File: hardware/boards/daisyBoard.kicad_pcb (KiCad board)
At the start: 4 copper layers, 100 x 100 mm, 93 parts, among them IC1 TL072, IC2 TL072, IC3 TL072, IC4 TL072, J1 LEFT Pin ROW, J12 Micro_SD_Card, J13 LEFT Pin ROW Daisy, J14 RIGHT Pin ROW DAISY, J15 Daisy Pin Breakout LEFT, J16 Daisy PIN Breakout RIGHT, J2 RIGHT Pin Row, J3 ESP32 Pin Breakout RIGHT, J4 ESP32 Pin Breakout LEFT, J5 Micro_SD_Card, U1 MCP6002-xSN, U2 MCP6002-xSN, U3 MCP6002-xSN

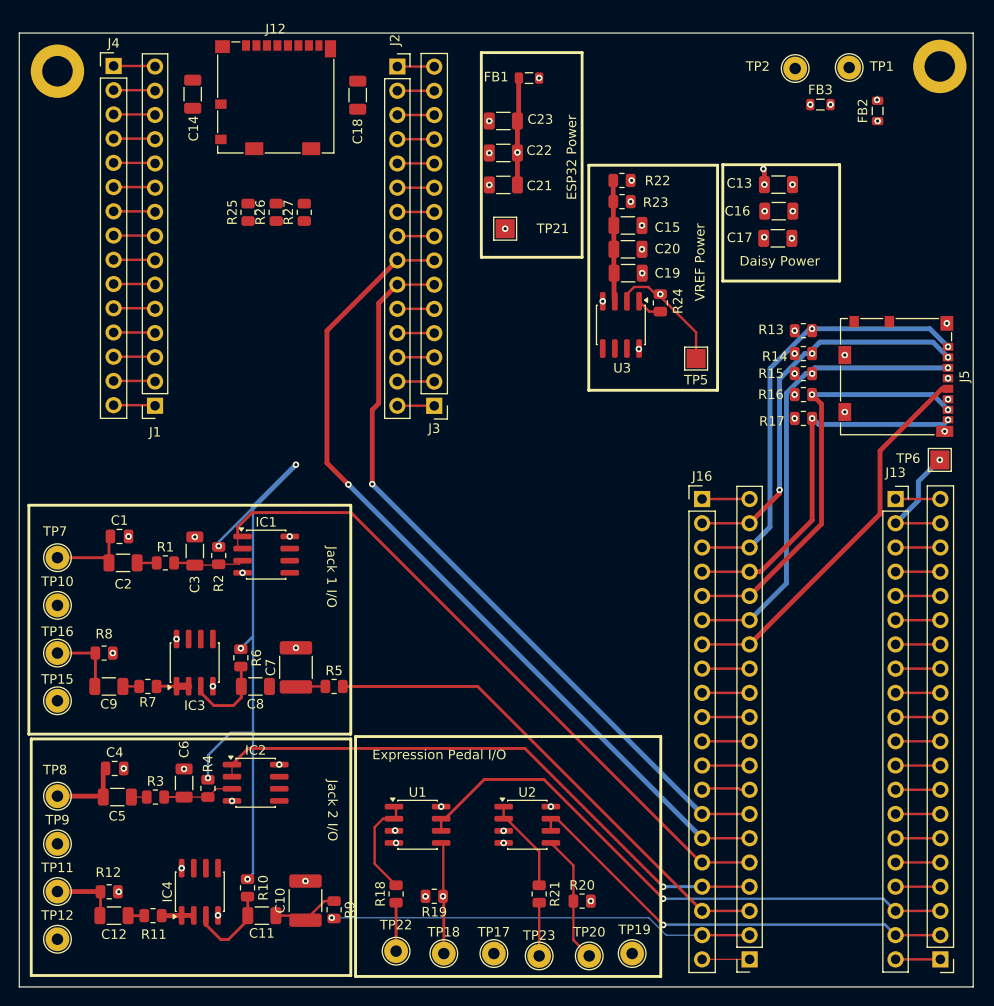
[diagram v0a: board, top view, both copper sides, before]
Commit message: Added compatible components
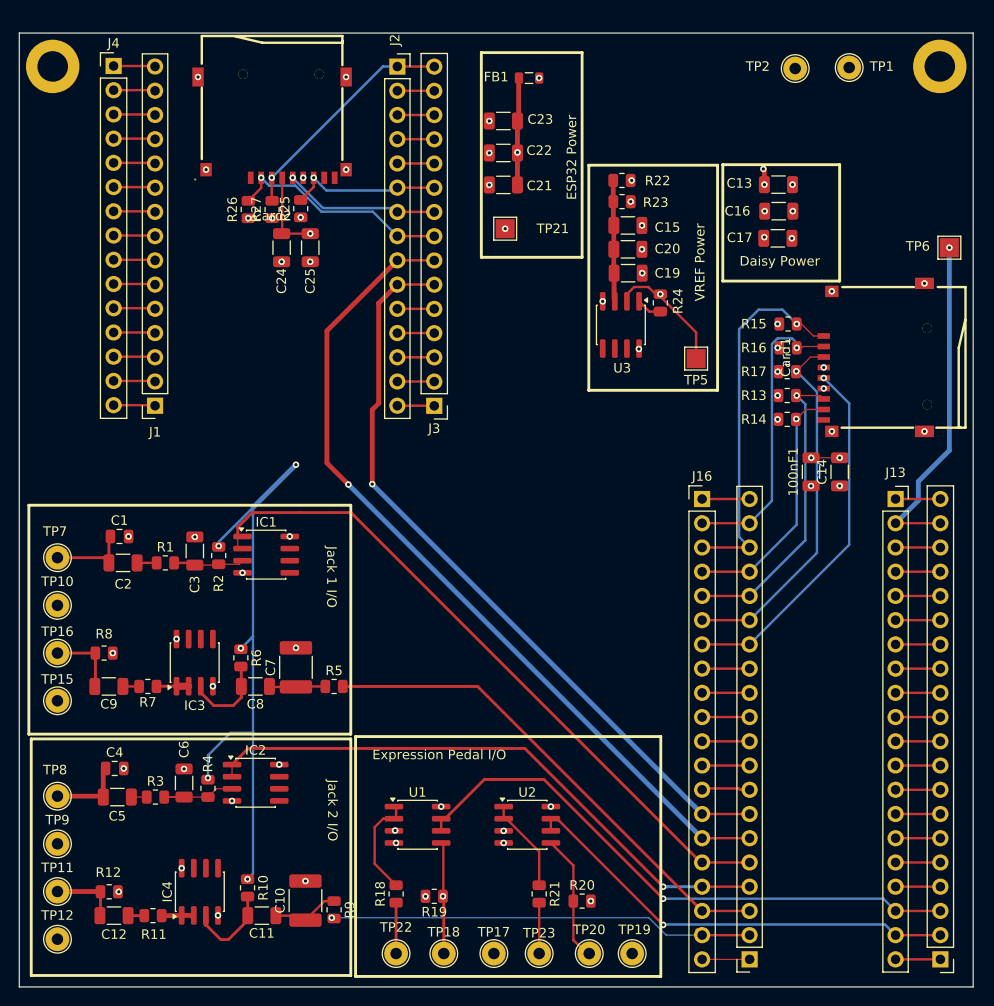
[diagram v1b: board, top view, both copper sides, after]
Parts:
- removed C18: 10uF, Capacitor_SMD:C_1206_3216Metric
- removed FB2, FB3: 600R @ 100MHz, Inductor_SMD:L_0805_2012Metric
- removed J12, J5: Micro_SD_Card, Connector_Card:microSD_HC_Molex_104031-0811
- added 100nF1: C26, Capacitor_SMD:C_1206_3216Metric, F.Cu at (133.0, 96.0)
- added C24: 10uF, Capacitor_SMD:C_1206_3216Metric, F.Cu at (77.5, 72.5)
- added C25: 100nF, Capacitor_SMD:C_1206_3216Metric, F.Cu at (80.5, 72.5)
- added Card1: TF-01A, lcsc_footprints:C91145_TF-SMD_TF-01A, F.Cu at (139.6, 84.0)
- added Card2: TF-01A, lcsc_footprints:C91145_TF-SMD_TF-01A, F.Cu at (76.5, 59.9)
- C14: value 0.1uF -> 10uF
- FB1: value 600R @ 100MHz -> 60R @ 100MHz
- R13, R14, R15, R16, R17, R25, R26, R27: value 10K -> 47K
- moved C14 78.5 mm to (136.0, 96.0)
- moved TP6 22.3 mm to (147.5, 72.5)
- moved R14 7.11 mm to (130.5, 90.5)
- moved R13 7.01 mm to (130.5, 88.0)
- moved R25 5.54 mm to (79.5, 68.4)
- moved R15 5.44 mm to (130.6, 80.5)
- moved R17 5.19 mm to (130.5, 85.5)
- moved R16 5.16 mm to (130.6, 83.0)
- moved R27 3.39 mm to (76.5, 68.5)
- moved R26 2.94 mm to (74.0, 68.5)
- moved REF** 0.71 mm to (53.5, 53.5)
- moved TP20 0.25 mm to (109.8, 146.5)
- moved TP22 0.25 mm to (89.5, 146.5)
- moved TP23 0.25 mm to (104.5, 146.5)
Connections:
- C1 pad 2: GNDA -> GND
- C10 pad 2: GNDA -> GND
- C13 pad 2: GNDA -> GND
- C14 pad 1: GNDD -> GND
- C14 pad 2: ESP-3.3V -> +3.3VD
- C15 pad 2: GNDA -> GND
- C16 pad 2: GNDA -> GND
- C17 pad 2: GNDA -> GND
- C19 pad 2: GNDA -> GND
- C20 pad 2: GNDA -> GND
- C21 pad 2: GNDD -> GND
- C22 pad 2: GNDD -> GND
- C23 pad 2: GNDD -> GND
- C3 pad 1: GNDA -> GND
- C4 pad 2: GNDA -> GND
- C6 pad 1: GNDA -> GND
- C7 pad 2: GNDA -> GND
- IC1 pad 4: GNDA -> GND
- IC2 pad 4: GNDA -> GND
- IC3 pad 4: GNDA -> GND
- IC4 pad 4: GNDA -> GND
- J1 pad 2: GNDD -> GND
- J13 pad 1: GNDA -> GND
- J14 pad 1: GNDA -> GND
- J15 pad 20: GNDA -> GND
- J16 pad 20: GNDA -> GND
- J2 pad 14: GNDD -> GND
- J3 pad 2: GNDD -> GND
- J4 pad 14: GNDD -> GND
- R12 pad 2: GNDA -> GND
- R13 pad 2: /SD_DAT_2_DAISY -> /SD_DAT_0_DAISY
- R14 pad 2: /SD_DAT_3_DAISY -> /SD_DAT_1_DAISY
- R15 pad 2: /SD_CMD_DAISY -> /SD_DAT_2_DAISY
- R16 pad 2: /SD_DAT_0_DAISY -> /SD_DAT_3_DAISY
- R17 pad 2: /SD_DAT_1_DAISY -> /SD_CMD_DAISY
- R19 pad 2: GNDA -> GND
- R20 pad 2: GNDA -> GND
- R23 pad 1: GNDA -> GND
- R25 pad 2: /SD_CS -> /SD_MISO
- R26 pad 2: /SD_MOSI -> /SD_CS
- R27 pad 2: /SD_MISO -> /SD_MOSI
- R8 pad 2: GNDA -> GND
- TP10 pad 1: GNDA -> GND
- TP12 pad 1: GNDA -> GND
- TP15 pad 1: GNDA -> GND
- TP17 pad 1: GNDA -> GND
- TP19 pad 1: GNDA -> GND
- TP9 pad 1: GNDA -> GND
- U1 pad 4: GNDA -> GND
- U2 pad 4: GNDA -> GND
- U3 pad 4: GNDA -> GND
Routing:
- net +3.3VD: track 41.5 -> 65.8 mm, vias 6 -> 8
- net VCC_Daisy: track 90.8 -> 111.3 mm
- net /SD_MOSI: track 3.87 -> 24.3 mm, vias 0 -> 1
- net /SD_CS: track 4.59 -> 24.4 mm, vias 0 -> 1
- net /SD_DAT_1_DAISY: track 40.2 -> 27.1 mm, vias 2 -> 1
- net /SD_DAT_0_DAISY: track 44.7 -> 32.0 mm, vias 2 -> 1
- net /SD_SCK: track 3.87 -> 16.3 mm, vias 0 -> 1
- net /SD_MISO: track 3.87 -> 16.2 mm, vias 0 -> 1
- net /SD_DAT_3_DAISY: track 41.7 -> 31.3 mm, vias 3 -> 1
- net /SD_CMD_DAISY: track 48.7 -> 38.5 mm, vias 2 -> 1
- net GNDA: track 9.74 -> 0.00 mm, vias 30 -> 0
- net GND: track 9.78 -> 18.5 mm, vias 2 -> 41
- net ESP-3.3V: track 3.87 -> 12.2 mm, vias 0 -> 4
- net GNDD: track 8.29 -> 0.00 mm, vias 4 -> 0
- net /SD_DAT_2_DAISY: track 46.4 -> 39.3 mm, vias 2 -> 1
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- added copper zone on In2.Cu, net GND
- removed copper zone on In1.Cu, net +3.3VD
- removed copper zone on In2.Cu, net GNDA
- removed copper zone on In2.Cu, net GNDD

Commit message: updated design and added start for indicator leds on design
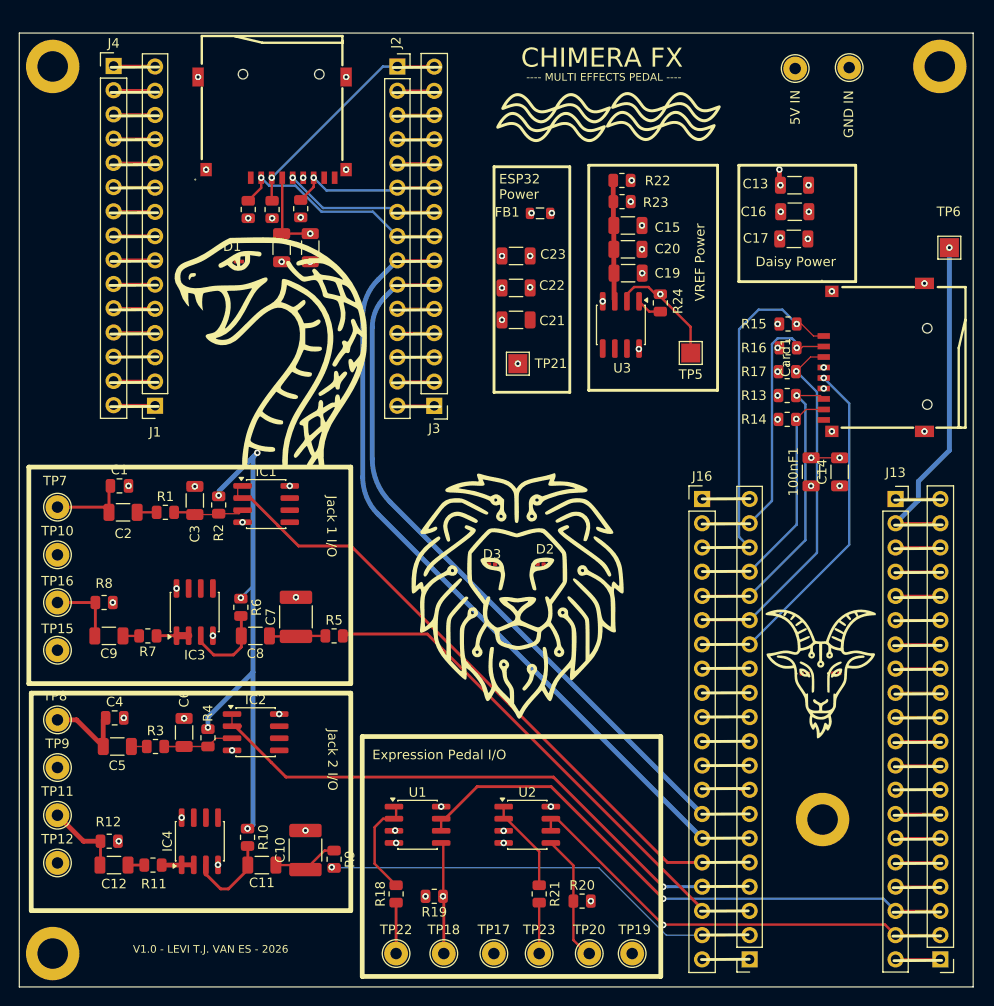
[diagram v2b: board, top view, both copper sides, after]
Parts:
- added D1: SNAKE EYE, LED_SMD:LED_0201_0603Metric, F.Cu at (73.0, 74.0)
- added D2: LION EYE 2, LED_SMD:LED_0201_0603Metric, F.Cu at (104.7, 105.7)
- added D3: LION EYE 1, LED_SMD:LED_0201_0603Metric, F.Cu at (99.6, 105.7)
- added D4: GOAT EYE 1, LED_SMD:LED_0201_0603Metric, F.Cu at (132.3, 117.2)
- added D5: GOAT EYE 2, LED_SMD:LED_0201_0603Metric, F.Cu at (135.6, 117.1)
- added G***: LOGO, LOGO, F.Cu at (105.8, 57.4)
- added G***: LOGO, LOGO, F.Cu at (133.8, 117.0)
- added G***: LOGO, LOGO, F.Cu at (116.7, 59.2)
- added G***: LOGO, LOGO, F.Cu at (117.3, 57.3)
- added G***: LOGO, LOGO, F.Cu at (105.2, 59.3)
- added G***: LOGO, LOGO, F.Cu at (76.6, 83.2)
- added G***: LOGO, LOGO, F.Cu at (101.8, 107.9)
- added REF**: MountingHole_3.2mm_M3_DIN965_Pad, MountingHole:MountingHole_3.2mm_M3_DIN965_Pad, F.Cu at (53.5, 146.5)
- added REF**: MountingHole_3.2mm_M3_DIN965_Pad, MountingHole:MountingHole_3.2mm_M3_DIN965_Pad, F.Cu at (134.2, 132.4)
- TP1: value Global Ground - Functional -> GND IN
- TP11: value Jack Output 2 Signal Pad -> Jack Output 2 Signal Pad test
- TP2: value Global power 5V Input field - Functional -> 5V IN
- moved FB1 14.2 mm to (104.6, 68.9)
- moved C23 14.2 mm to (102.1, 73.4)
- moved C21 14.2 mm to (102.1, 80.1)
- moved C22 14.2 mm to (102.1, 76.7)
- moved TP21 14.2 mm to (102.3, 84.7)
- moved TP11 8.00 mm to (54.0, 132.0)
- moved TP12 8.00 mm to (54.0, 137.0)
- moved TP8 8.00 mm to (54.0, 122.0)
- moved TP9 8.00 mm to (54.0, 127.0)
- moved C1 5.30 mm to (60.5, 97.5)
- moved C11 5.30 mm to (75.4, 137.2)
- moved C12 5.30 mm to (59.9, 137.2)
- moved C6 5.30 mm to (67.3, 123.3)
- moved IC1 5.30 mm to (75.9, 99.4)
- moved IC4 5.30 mm to (68.9, 134.7)
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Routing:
- net VCC_ESP32: track 86.4 -> 68.2 mm, vias 2 -> 4
- net +5V: track 81.8 -> 93.1 mm
- net /ESP_TO_DAISY: track 88.9 -> 85.2 mm, vias 1 -> 0
- net VREF: track 123.7 -> 120.9 mm
- net /AUDIO_OUT_1: track 52.5 -> 55.1 mm
- net /AUDIO_OUT_2: track 45.4 -> 47.6 mm
- net /AUDIO_IN_1: track 71.8 -> 70.3 mm
- net VCC_Daisy: track 111.3 -> 112.7 mm
- net /AUDIO_IN_2: track 62.3 -> 63.5 mm
- net Net-(C12-Pad2): track 7.05 -> 8.20 mm
- net Net-(C4-Pad1): track 7.94 -> 9.06 mm
- net /ADC_EXP_IN_1: track 61.4 -> 60.8 mm
- net /DAISY_TO_ESP: track 79.8 -> 79.3 mm, vias 1 -> 0
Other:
- board text added: "---- MULTI EFFECTS PEDAL ----"
- board text added: "CHIMERA FX"
- board text added: "V1.0 - LEVI T.J. VAN ES - 2026"

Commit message: removed grbrs and updated corner design pcb and still need to add led resistors
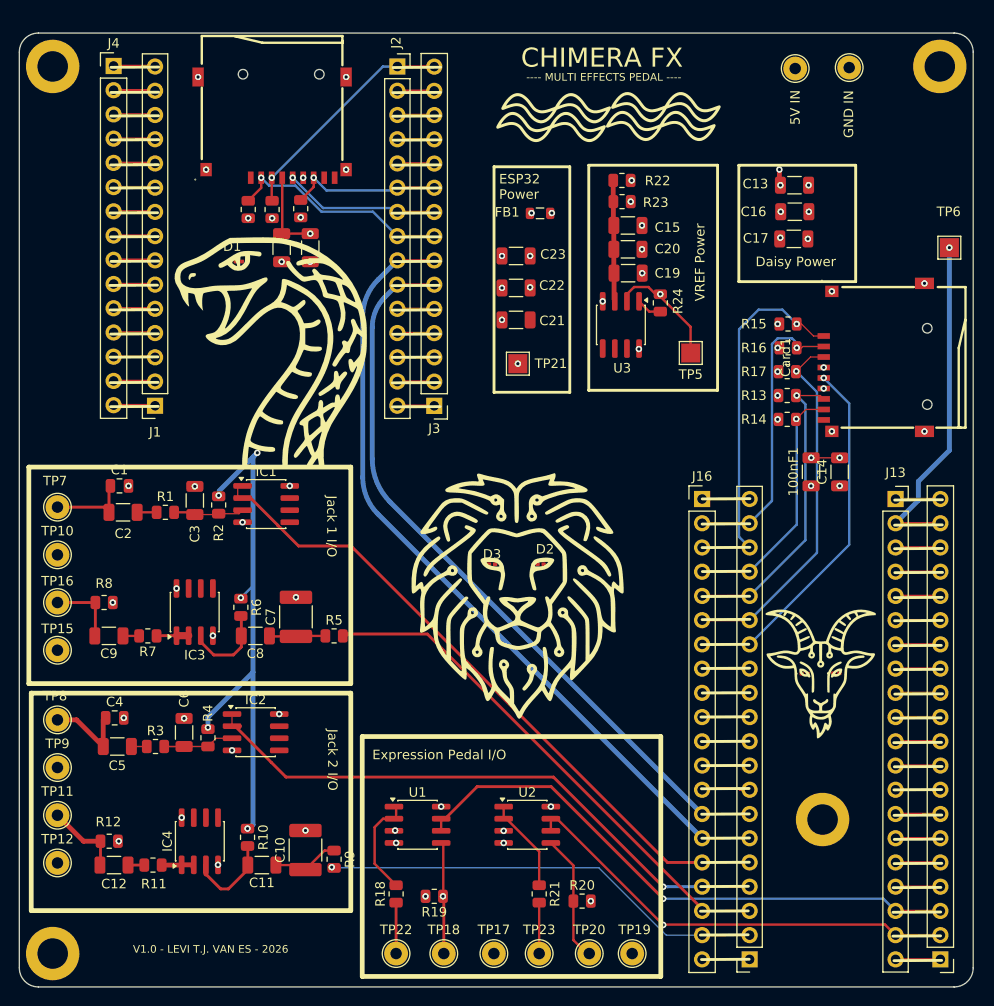
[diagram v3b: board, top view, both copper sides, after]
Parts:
- D1: value SNAKE EYE -> SNAKE EYE - GREEN
- D2: value LION EYE 2 -> LION EYE 2 - YELLOW
- D3: value LION EYE 1 -> LION EYE 1 - YELLOW
- D4: value GOAT EYE 1 -> GOAT EYE 1 - RED
- D5: value GOAT EYE 2 -> GOAT EYE 2 - RED
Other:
- outline, holes or cut-outs redrawn

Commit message: added led values
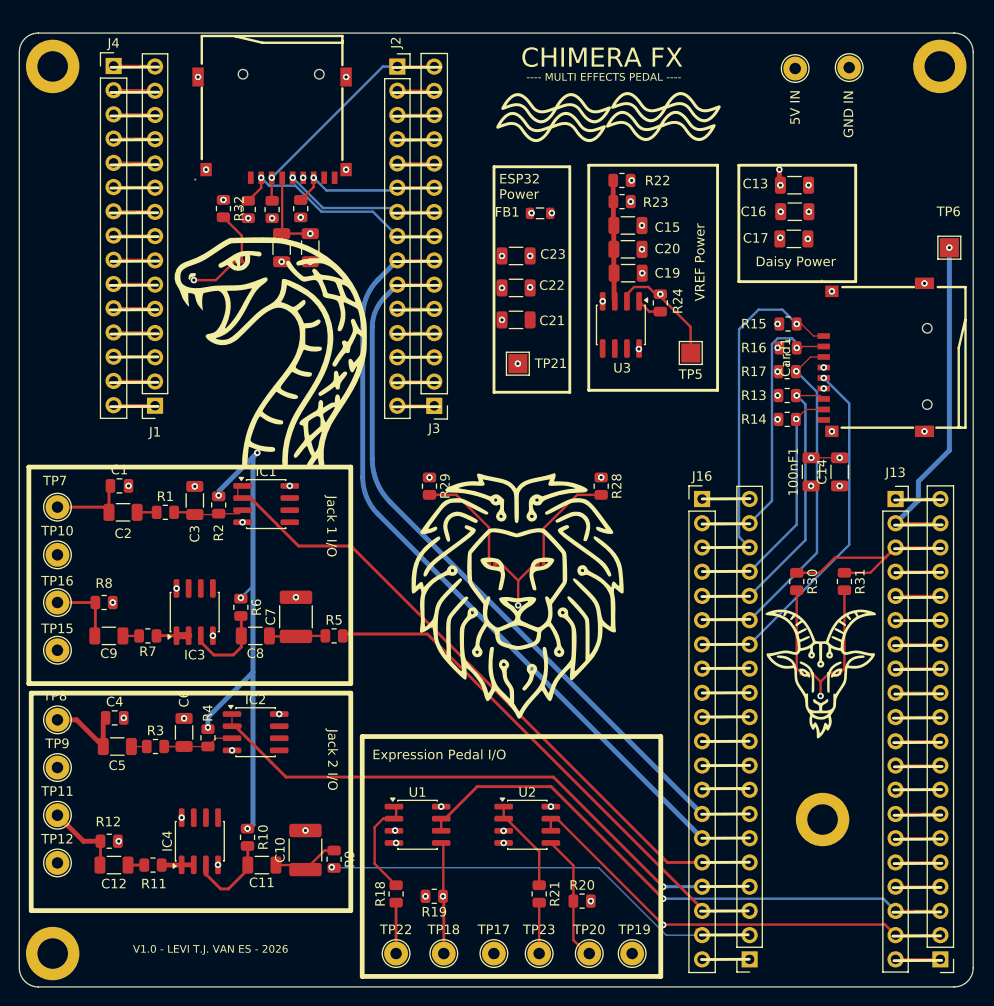
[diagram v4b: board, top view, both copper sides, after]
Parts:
- added R28: 150, Resistor_SMD:R_0805_2012Metric, F.Cu at (111.0, 97.5)
- added R29: 150, Resistor_SMD:R_0805_2012Metric, F.Cu at (93.0, 97.5)
- added R30: 120, Resistor_SMD:R_0805_2012Metric, F.Cu at (131.5, 107.5)
- added R31: 120, Resistor_SMD:R_0805_2012Metric, F.Cu at (136.5, 107.5)
- added R32: 27, Resistor_SMD:R_0805_2012Metric, F.Cu at (71.4, 68.4)
- D2: value LION EYE 2 - YELLOW -> LION EYE 2 - RED
- D3: value LION EYE 1 - YELLOW -> LION EYE 1 - RED
- D4: value GOAT EYE 1 - RED -> GOAT EYE 1 - YELLOW
- D5: value GOAT EYE 2 - RED -> GOAT EYE 2 - YELLOW
- R5, R9: value 3R3 -> 3K3
- TP21: value Processed input power at 5V ESP32 - Probe -> VCC_ESP32_Probe
- TP6: value Processed input power at 5V Daisy- Probe -> VCC Daisy Probe
- turned D3 to 180 degrees
- turned D4 to 180 degrees
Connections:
- D1 pad 2: ESP-3.3V -> Net-(D1-A)
- D2 pad 2: VCC_Daisy -> Net-(D2-A)
- D3 pad 2: VCC_Daisy -> Net-(D3-A)
- D4 pad 2: +3.3VD -> Net-(D4-A)
- D5 pad 2: +3.3VD -> Net-(D5-A)
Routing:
- net GND: track 18.5 -> 37.0 mm, vias 41 -> 44
- net +3.3VD: track 65.8 -> 83.3 mm
- net Net-(D3-A): track 0.00 -> 11.5 mm
- net Net-(D2-A): track 0.00 -> 11.2 mm
- net Net-(D4-A): track 0.00 -> 8.95 mm
- net Net-(D5-A): track 0.00 -> 8.93 mm
- net Net-(D1-A): track 0.00 -> 5.44 mm
- net VCC_Daisy: vias 10 -> 12
- net ESP-3.3V: vias 4 -> 5

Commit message: updated missing pcb connection
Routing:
- net VCC_ESP32: vias 4 -> 5
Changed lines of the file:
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@@
 				(font
 					(size 1.27 1.27)
+					(thickness 0.15)
 				)
 			)
@@
 				(font
 					(size 1.27 1.27)
+					(thickness 0.15)
 				)
 			)
@@
 				(font
 					(size 1.27 1.27)
+					(thickness 0.15)
 				)
 			)
@@
 				(font
 					(size 1.27 1.27)
+					(thickness 0.15)
 				)
 			)
@@
 				(font
 					(size 1.27 1.27)
+					(thickness 0.15)
 				)
 			)
@@
 				(font
 					(size 1.27 1.27)
+					(thickness 0.15)
 				)
 			)
@@
 				(font
 					(size 1.27 1.27)
+					(thickness 0.15)
 				)
 			)
@@
 	)
 	(via
+		(at 103.322434 79.822434)
+		(size 0.6858)
+		(drill 0.3302)
+		(layers "F.Cu" "B.Cu")
+		(net "VCC_ESP32")
+	)
+	(via
 		(at 102.265 84.66)
 		(size 0.6858)
@@
 	)
 	(segment
-		(start 103.55 79.594868)
+		(start 103.322434 79.822434)
 		(end 100.090559 83.054309)
 		(width 0.762)
 		(layer "In1.Cu")
+		(net "VCC_ESP32")
+	)
+	(segment
+		(start 103.55 79.594868)
+		(end 103.322434 79.822434)
+		(width 0.762)
+		(layer "In1.Cu")
